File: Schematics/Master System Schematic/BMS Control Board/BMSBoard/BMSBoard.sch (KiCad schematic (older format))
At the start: 12 parts, among them K1 Relay_NC, K2 Relay_NO, K3 Relay_NO, K4 Relay_NO

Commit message: Quick fix
> Noticed and deleted BMSIn12V line, would be the same as PWR_Ready
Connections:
- net BMSIn12V renamed GLV_BMSContainer
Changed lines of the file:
@@
 EESchema Schematic File Version 4
-LIBS:BMSBoard-cache
 EELAYER 30 0
 EELAYER END
@@
 Text GLabel 1550 1900 2    50   Input ~ 0
 CANH_Main
+Text GLabel 9650 1850 0    50   Input ~ 0
+CANS_BMS
 Text GLabel 9650 1700 0    50   Input ~ 0
-CANS_BMS
+CANL_BMS
 Text GLabel 9650 1550 0    50   Input ~ 0
-CANL_BMS
-Text GLabel 9650 1400 0    50   Input ~ 0
 CANH_BMS
-Text GLabel 9650 1850 0    50   Input ~ 0
-BMSIn12V
 Text GLabel 9650 2000 0    50   Input ~ 0
 BMSGND
@@
 ThermEx
 Entry Wire Line
+	9850 2100 9750 2000
+Entry Wire Line
+	9850 2250 9750 2150
+Entry Wire Line
+	9850 2400 9750 2300
+Entry Wire Line
+	9850 2550 9750 2450
+Entry Wire Line
+	9850 2700 9750 2600
+Wire Wire Line
+	9750 2000 9650 2000
+Wire Wire Line
+	9750 2150 9650 2150
+Wire Wire Line
+	9750 2300 9650 2300
+Wire Wire Line
+	9750 2450 9650 2450
+Wire Wire Line
+	9750 2600 9650 2600
+Entry Wire Line
+	9850 1650 9750 1550
+Entry Wire Line
+	9850 1800 9750 1700
+Entry Wire Line
 	9850 1950 9750 1850
-Entry Wire Line
-	9850 2100 9750 2000
-Entry Wire Line
-	9850 2250 9750 2150
-Entry Wire Line
-	9850 2400 9750 2300
-Entry Wire Line
-	9850 2550 9750 2450
-Entry Wire Line
-	9850 2700 9750 2600
+Wire Wire Line
+	9750 1550 9650 1550
+Wire Wire Line
+	9750 1700 9650 1700
 Wire Wire Line
 	9750 1850 9650 1850
-Wire Wire Line
-	9750 2000 9650 2000
-Wire Wire Line
-	9750 2150 9650 2150
-Wire Wire Line
-	9750 2300 9650 2300
-Wire Wire Line
-	9750 2450 9650 2450
-Wire Wire Line
-	9750 2600 9650 2600
-Entry Wire Line
-	9850 1500 9750 1400
-Entry Wire Line
-	9850 1650 9750 1550
-Entry Wire Line
-	9850 1800 9750 1700
-Wire Wire Line
-	9750 1400 9650 1400
-Wire Wire Line
-	9750 1550 9650 1550
-Wire Wire Line
-	9750 1700 9650 1700
 Text HLabel 10100 2700 2    50   Input ~ 0
 BMS
@@
 Text GLabel 7000 4350 2    50   Input ~ 0
 ThermExIn12V
-Text GLabel 7000 4500 2    50   Input ~ 0
-BMSIn12V
 Wire Wire Line
 	6800 4200 6900 4200
@@
 Wire Wire Line
 	6900 4350 6900 4200
-Wire Wire Line
-	7000 4500 6900 4500
-Wire Wire Line
-	6900 4500 6900 4350
-Connection ~ 6900 4350
 Text GLabel 6550 4800 0    50   Input ~ 0
 ChassisGND
@@
 	3600 4400 3700 4400
 Connection ~ 4400 4400
-Text GLabel 7000 4650 2    50   Input ~ 0
+Text GLabel 7000 4500 2    50   Input ~ 0
 PWR_Ready
-Wire Wire Line
-	6900 4500 6900 4650
-Wire Wire Line
-	6900 4650 7000 4650
-Connection ~ 6900 4500
 Wire Notes Line
 	5950 6000 8950 6000
@@
 GLV_BMSContainer
 Entry Wire Line
-	9850 1350 9750 1250
-Wire Wire Line
-	9750 1250 9650 1250
-Text GLabel 9650 1250 0    50   Input ~ 0
+	9850 1500 9750 1400
+Wire Wire Line
+	9750 1400 9650 1400
+Text GLabel 9650 1400 0    50   Input ~ 0
 MPOut3
 Text GLabel 8050 2050 2    50   Input ~ 0
@@
 Wire Bus Line
 	1100 6000 1350 6000
+Wire Wire Line
+	6900 4350 6900 4500
+Wire Wire Line
+	6900 4500 7000 4500
 Wire Bus Line
 	1350 5400 1350 6000
@@
 	1350 1550 1350 2300
 Wire Bus Line
-	9850 1350 9850 2700
+	9850 1500 9850 2700
+Connection ~ 6900 4350
 $EndSCHEMATC

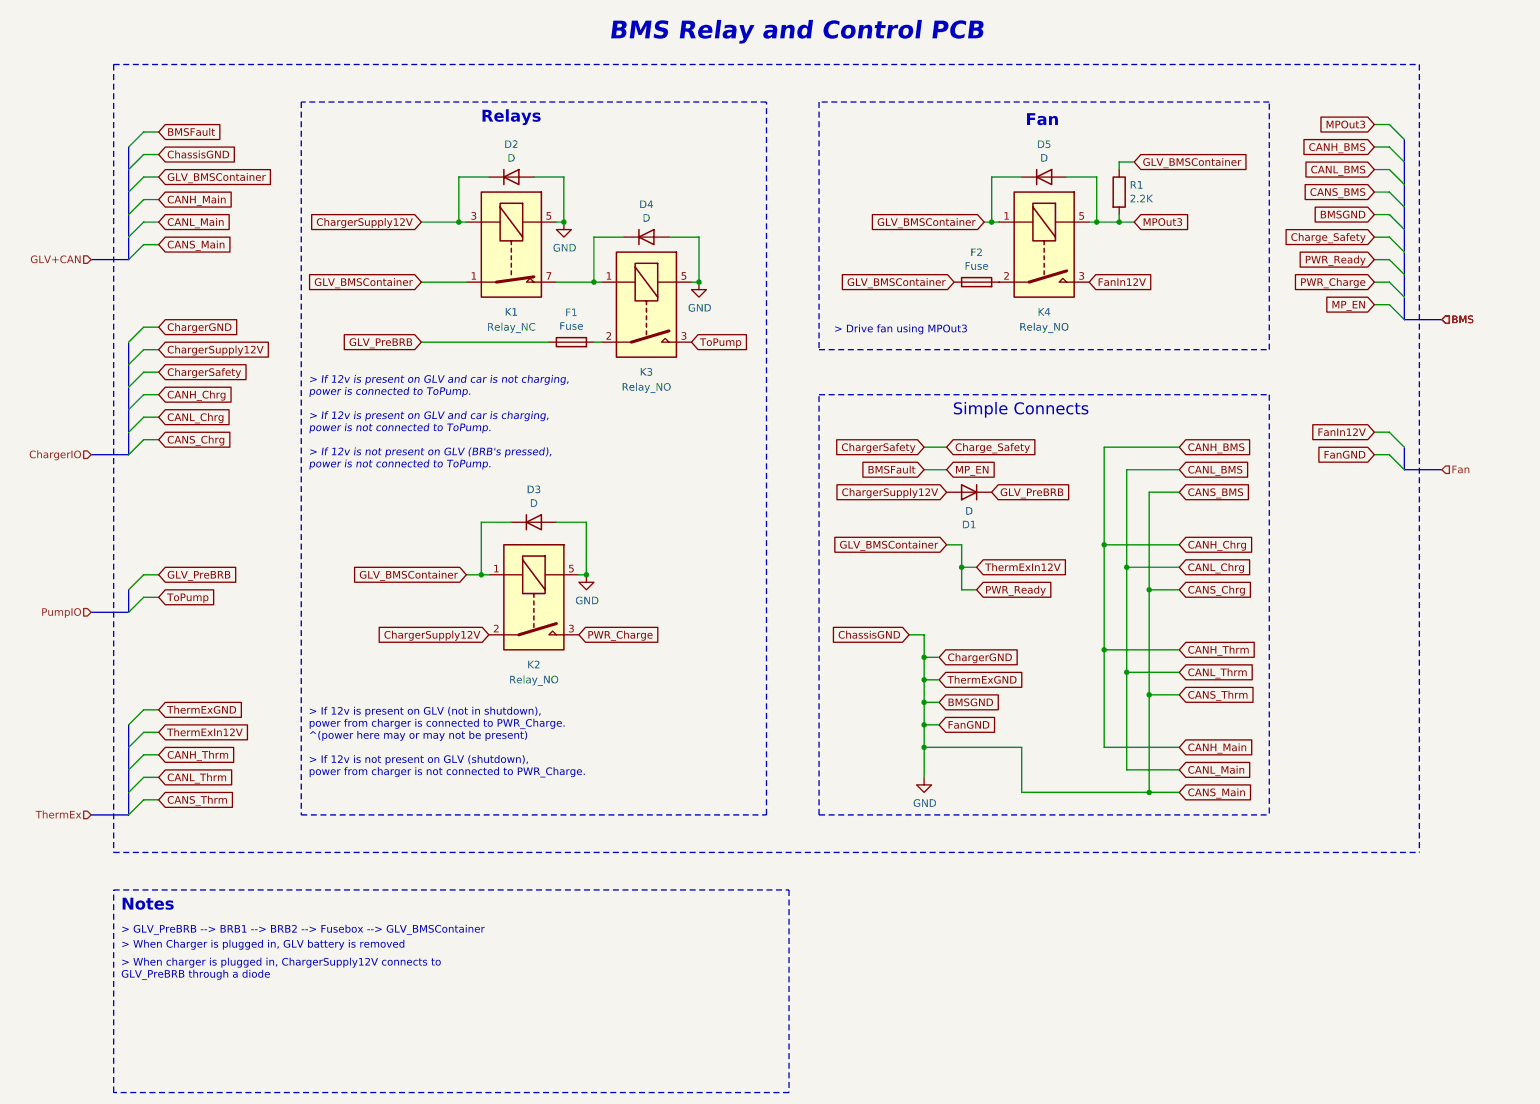
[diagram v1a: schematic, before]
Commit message: BMS Control Board V2
> Fan relay removed, BMS will be passively cooled.
> Ground sourced from chassis through quick connect spade connector.
> Diode from Charger Power to GLV replaced with a relay.
> Connectors added for all control board IO.
> Fusing to be added later today.
Version 2
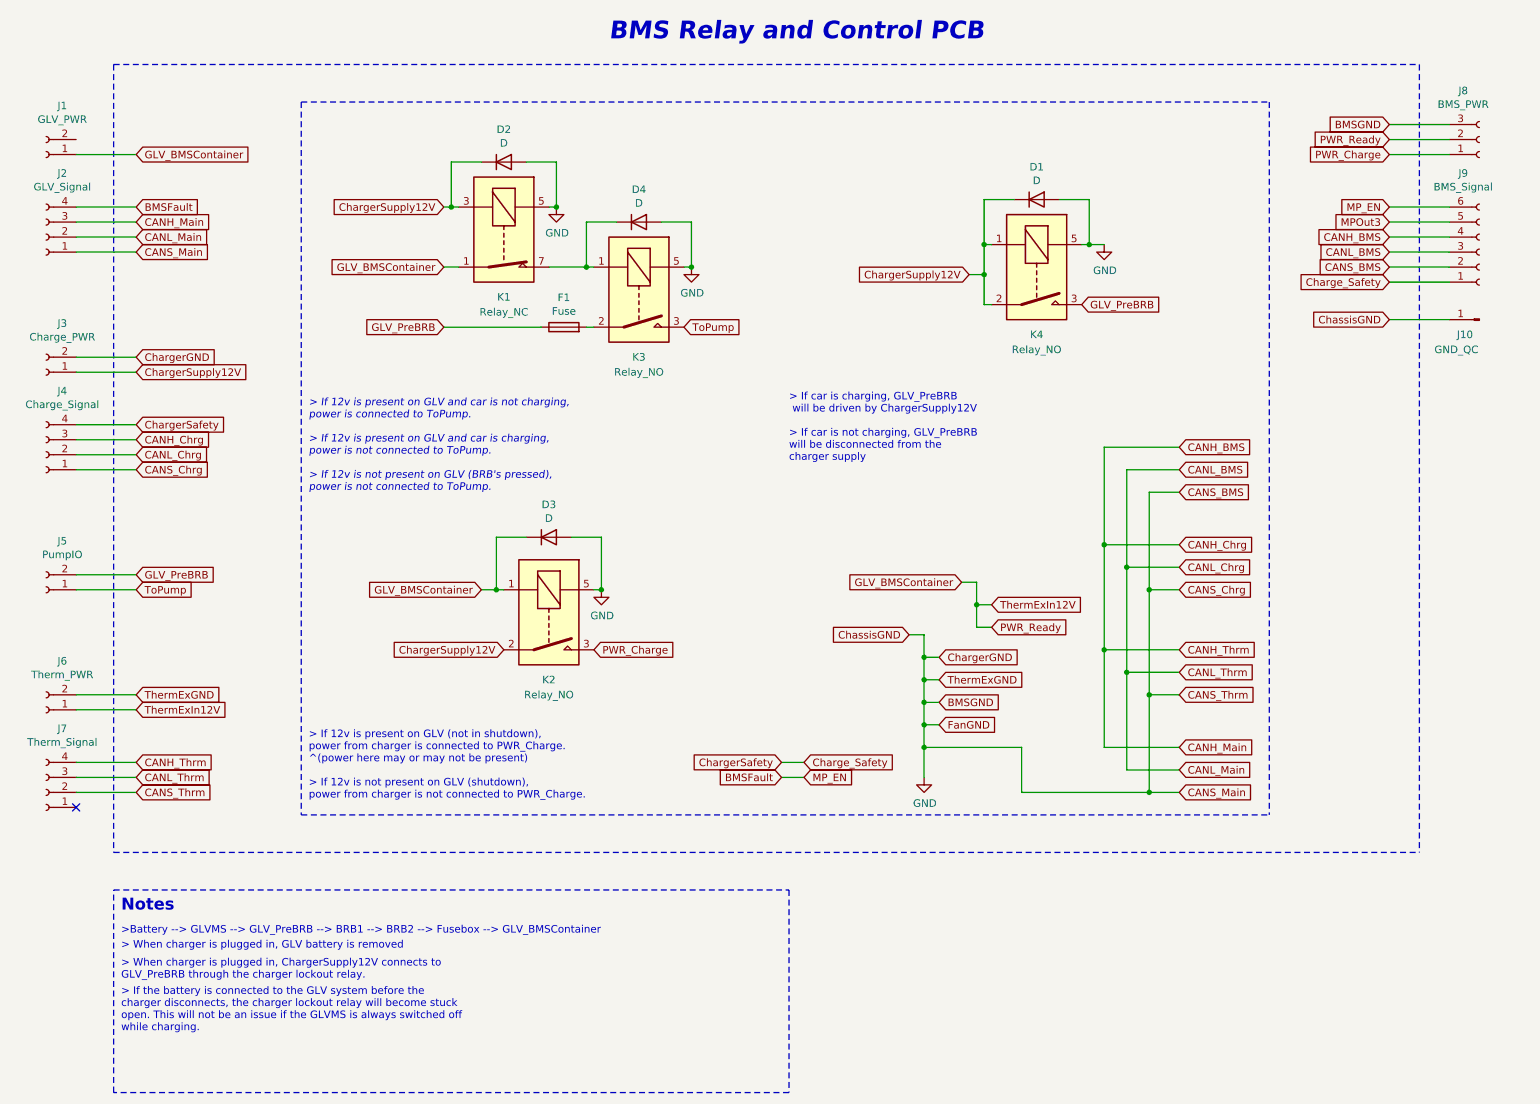
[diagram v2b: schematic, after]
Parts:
- removed D5: D, symbol Device:D
- removed F2: Fuse, symbol Device:Fuse
- removed R1: 2.2K, symbol Device:R
- added J1: GLV_PWR, symbol Connector:Conn_01x02_Female
- added J10: GND_QC, symbol Connector:Conn_01x01_Male
- added J2: GLV_Signal, symbol Connector:Conn_01x04_Female
- added J3: Charge_PWR, symbol Connector:Conn_01x02_Female
- added J4: Charge_Signal, symbol Connector:Conn_01x04_Female
- added J5: PumpIO, symbol Connector:Conn_01x02_Female
- added J6: Therm_PWR, symbol Connector:Conn_01x02_Female
- added J7: Therm_Signal, symbol Connector:Conn_01x04_Female
- added J8: BMS_PWR, symbol Connector:Conn_01x03_Female
- added J9: BMS_Signal, symbol Connector:Conn_01x06_Female
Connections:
- net FanIn12V is gone; now on net GLV_PreBRB: K4.3
- net BMSFault: now also J2.4 (Pin_4), J9.6 (Pin_6)
- net CANH_BMS: now also J2.3 (Pin_3), J4.3 (Pin_3), J7.4 (Pin_4), J9.4 (Pin_4)
- net CANL_BMS: now also J2.2 (Pin_2), J4.2 (Pin_2), J7.3 (Pin_3), J9.3 (Pin_3)
- net Charge_Safety: now also J4.4 (Pin_4), J9.1 (Pin_1)
- net ChargerSupply12V: now also D1.1 (K), K4.1, K4.2, J3.1 (Pin_1); no longer D1.2 (A)
- net GLV_BMSContainer: now also J1.1 (Pin_1), J6.1 (Pin_1), J8.2 (Pin_2); no longer K4.1
- net GLV_PreBRB: now also J5.2 (Pin_2); no longer D1.1 (K)
- net GND: now also D1.2 (A), K4.5, J10.1 (Pin_1), J2.1 (Pin_1), J3.2 (Pin_2), J4.1 (Pin_1), J6.2 (Pin_2), J7.2 (Pin_2), J8.3 (Pin_3), J9.2 (Pin_2)
- net MPOut3: now also J9.5 (Pin_5); no longer K4.5
- net PWR_Charge: now also J8.1 (Pin_1)
- net ToPump: now also J5.1 (Pin_1)
- no-connect marks 0 -> 1
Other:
- note added: "> If car is charging, GLV_PreBRB\n will be driven by ChargerSupply12V\n\n> If car is not charging, GLV_PreBRB \nwill be disconnected from the \ncharger supply"
- note added: "> If the battery is connected to the GLV system before the\ncharger disconnects, the charger lockout relay will become stuck\nopen. This will not be an issue if the GLVMS is always switched off\nwhile charging."
- note added: "> When charger is plugged in, ChargerSupply12V connects to \nGLV_PreBRB through the charger lockout relay.\n"
- note added: "> When charger is plugged in, GLV battery is removed\n"
- note added: ">Battery --> GLVMS --> GLV_PreBRB --> BRB1 --> BRB2 --> Fusebox --> GLV_BMSContainer\n"
- note removed: "> Drive fan using MPOut3"
- note removed: "> GLV_PreBRB --> BRB1 --> BRB2 --> Fusebox --> GLV_BMSContainer\n"
- note removed: "> When Charger is plugged in, GLV battery is removed\n"
- note removed: "> When charger is plugged in, ChargerSupply12V connects to \nGLV_PreBRB through a diode"
- note removed: "Fan\n\n"
- note removed: "Relays\n"
- note removed: "Simple Connects\n"
- moved on the sheet: D2, D3, D4, F1, K1, K2, K3

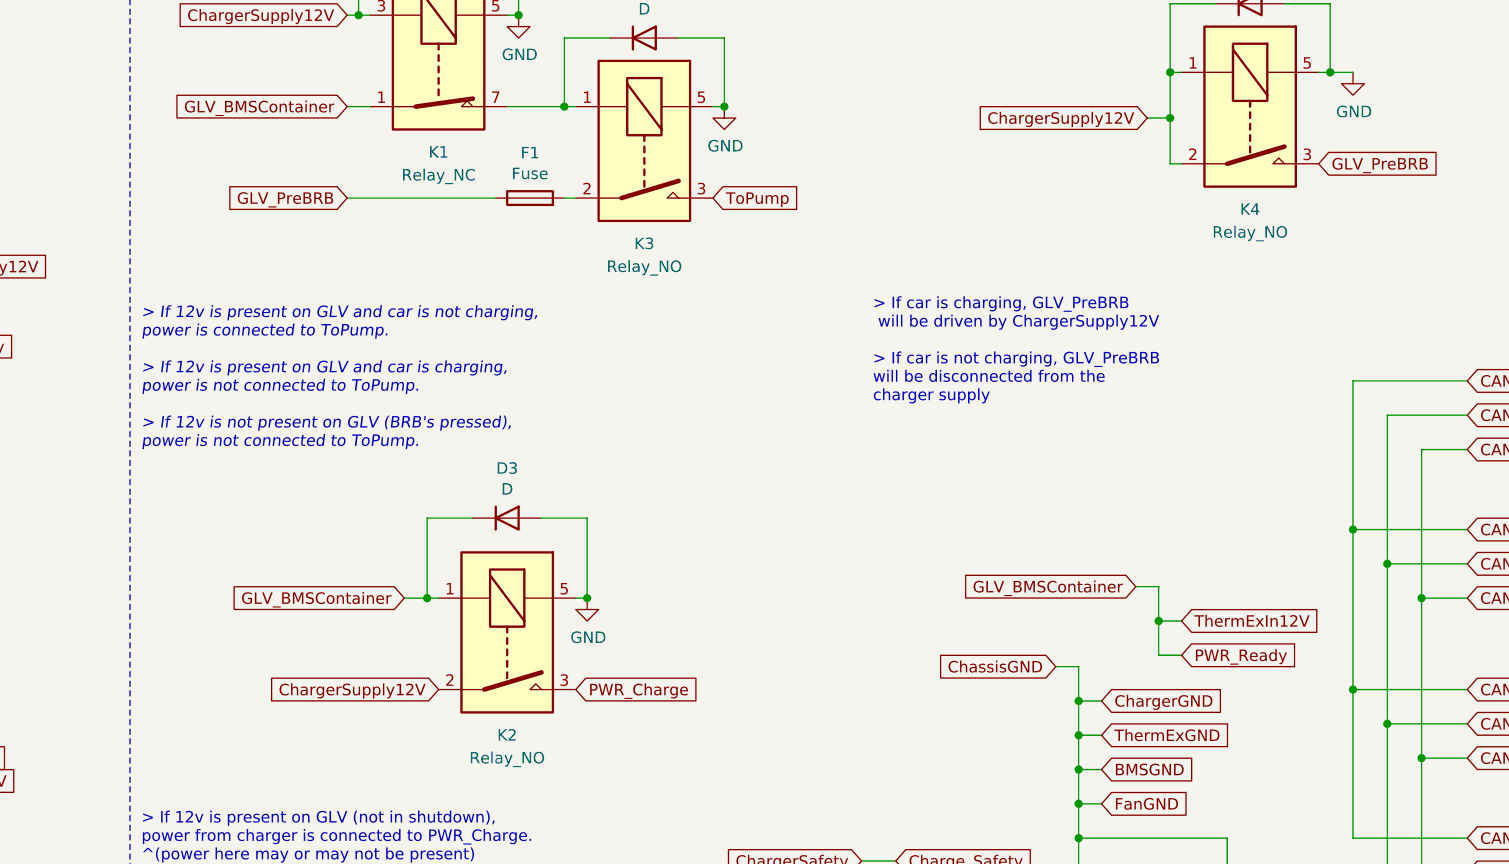
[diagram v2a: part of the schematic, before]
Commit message: Fusing
> Added fuses for pump, pwr_charge, pwr_ready, and thermistor expansion.
> Minor fixes
Version 2.1
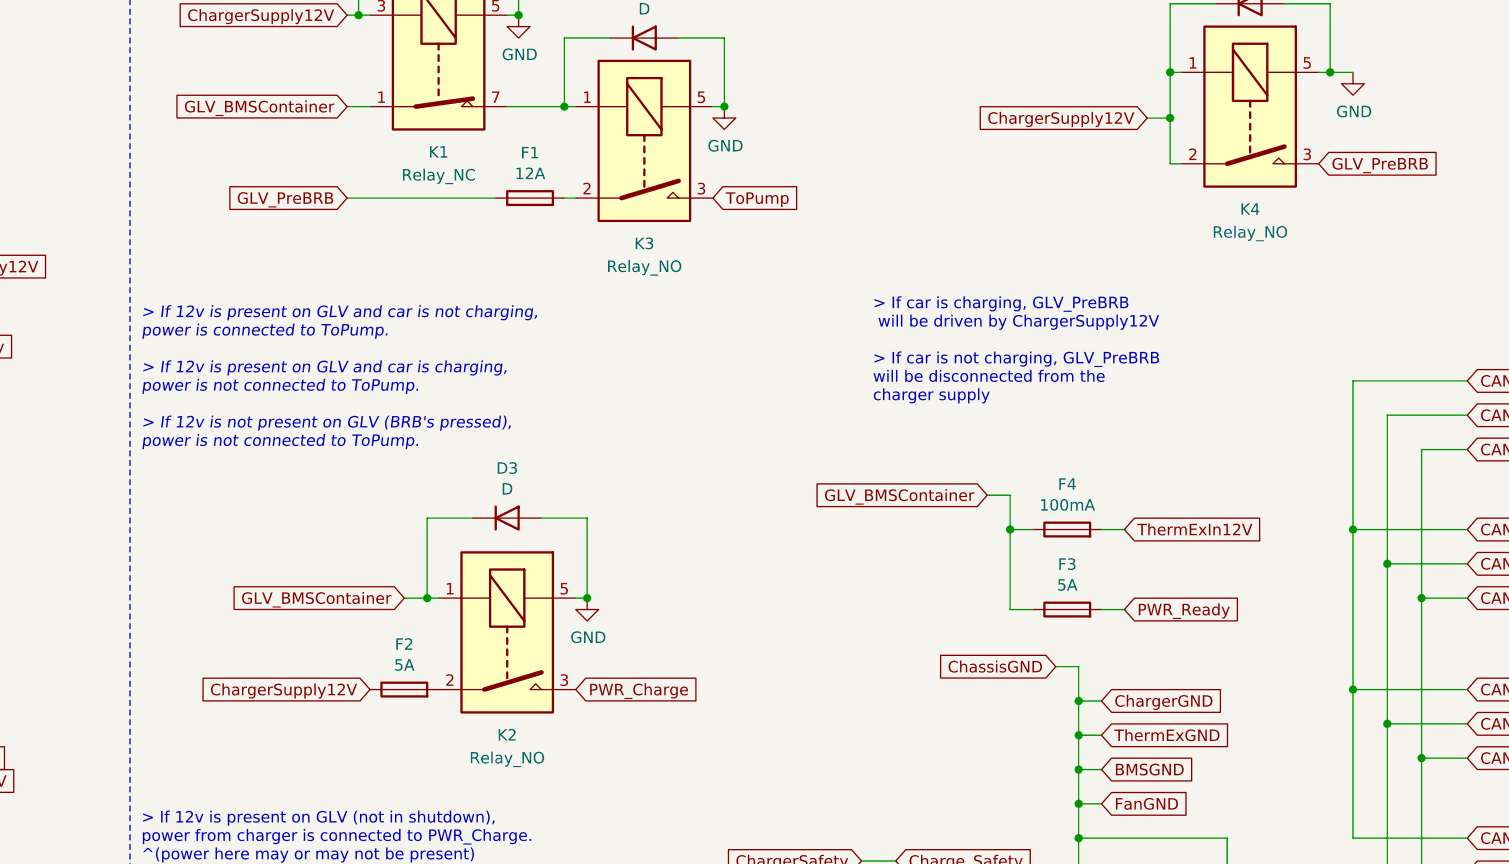
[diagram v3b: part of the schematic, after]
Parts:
- added F2, F3: 5A, symbol Device:Fuse
- added F4: 100mA, symbol Device:Fuse
- F1: value Fuse -> 12A
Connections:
- net ChargerSupply12V: now also F2.1; no longer K2.2
- net GLV_BMSContainer: now also F3.1, F4.1; no longer J6.1 (Pin_1), J8.2 (Pin_2)
- new net: F2.2, K2.2
- new net PWR_Ready: F3.2, J8.2 (Pin_2)
- new net ThermExIn12V: F4.2, J6.1 (Pin_1)
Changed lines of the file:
@@
 Title "BMS Control Board"
 Date "2020-11-14"
-Rev "2"
+Rev "2.1"
 Comp "Northeastern Electric Racing"
 Comment1 "https://github.com/Northeastern-Electric-Racing/NER"
@@
 Wire Wire Line
 	5700 5750 5850 5750
-Text GLabel 6900 4450 0    50   Input ~ 0
+Text GLabel 6250 4050 0    50   Input ~ 0
 GLV_BMSContainer
-Text GLabel 7100 4600 2    50   Input ~ 0
+Text GLabel 6850 4200 2    50   Input ~ 0
 ThermExIn12V
 Wire Wire Line
-	6900 4450 7000 4450
-Wire Wire Line
-	7100 4600 7000 4600
-Wire Wire Line
-	7000 4600 7000 4450
+	6250 4050 6350 4050
+Wire Wire Line
+	6450 4200 6350 4200
+Wire Wire Line
+	6350 4200 6350 4050
 Text GLabel 6550 4800 0    50   Input ~ 0
 ChassisGND
@@
 Wire Notes Line
 	2500 1250 2500 6000
-Text GLabel 3850 4900 0    50   Input ~ 0
+Text GLabel 3550 4900 0    50   Input ~ 0
 ChargerSupply12V
 Text GLabel 4450 4900 2    50   Input ~ 0
@@
 	3700 4500 3800 4500
 Connection ~ 4500 4500
-Text GLabel 7100 4750 2    50   Input ~ 0
+Text GLabel 6850 4550 2    50   Input ~ 0
 PWR_Ready
 Wire Wire Line
@@
 P 4250 2750
 F 0 "F1" V 4447 2750 50  0000 C CNN
-F 1 "Fuse" V 4356 2750 50  0000 C CNN
+F 1 "12A" V 4356 2750 50  0000 C CNN
 F 2 "" V 4180 2750 50  0001 C CNN
 F 3 "~" H 4250 2750 50  0001 C CNN
@@
 Text Notes 2550 5900 0    50   ~ 0
 > If 12v is present on GLV (not in shutdown), \npower from charger is connected to PWR_Charge.\n^(power here may or may not be present)\n\n> If 12v is not present on GLV (shutdown),\npower from charger is not connected to PWR_Charge.
-Wire Wire Line
-	7000 4600 7000 4750
-Wire Wire Line
-	7000 4750 7100 4750
-Connection ~ 7000 4600
+Connection ~ 6350 4200
 $Comp
 L Relay:G5Q-1A K4
@@
 	-1   0    0    -1
 $EndComp
+$Comp
+L Device:Fuse F2
+U 1 1 5FB0792D
+P 3700 4900
+F 0 "F2" V 3897 4900 50  0000 C CNN
+F 1 "5A" V 3806 4900 50  0000 C CNN
+F 2 "" V 3630 4900 50  0001 C CNN
+F 3 "~" H 3700 4900 50  0001 C CNN
+	1    3700 4900
+	0    -1   -1   0
+$EndComp
+$Comp
+L Device:Fuse F3
+U 1 1 5FB100A8
+P 6600 4550
+F 0 "F3" V 6797 4550 50  0000 C CNN
+F 1 "5A" V 6706 4550 50  0000 C CNN
+F 2 "" V 6530 4550 50  0001 C CNN
+F 3 "~" H 6600 4550 50  0001 C CNN
+	1    6600 4550
+	0    -1   -1   0
+$EndComp
+Wire Wire Line
+	6350 4550 6450 4550
+Wire Wire Line
+	6350 4200 6350 4550
+Wire Wire Line
+	6750 4550 6850 4550
+$Comp
+L Device:Fuse F4
+U 1 1 5FB1D8F5
+P 6600 4200
+F 0 "F4" V 6797 4200 50  0000 C CNN
+F 1 "100mA" V 6706 4200 50  0000 C CNN
+F 2 "" V 6530 4200 50  0001 C CNN
+F 3 "~" H 6600 4200 50  0001 C CNN
+	1    6600 4200
+	0    -1   -1   0
+$EndComp
+Wire Wire Line
+	6750 4200 6850 4200
 $EndSCHEMATC
